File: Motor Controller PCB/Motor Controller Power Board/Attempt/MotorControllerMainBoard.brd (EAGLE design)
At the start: 70 x 100 mm, 47 parts

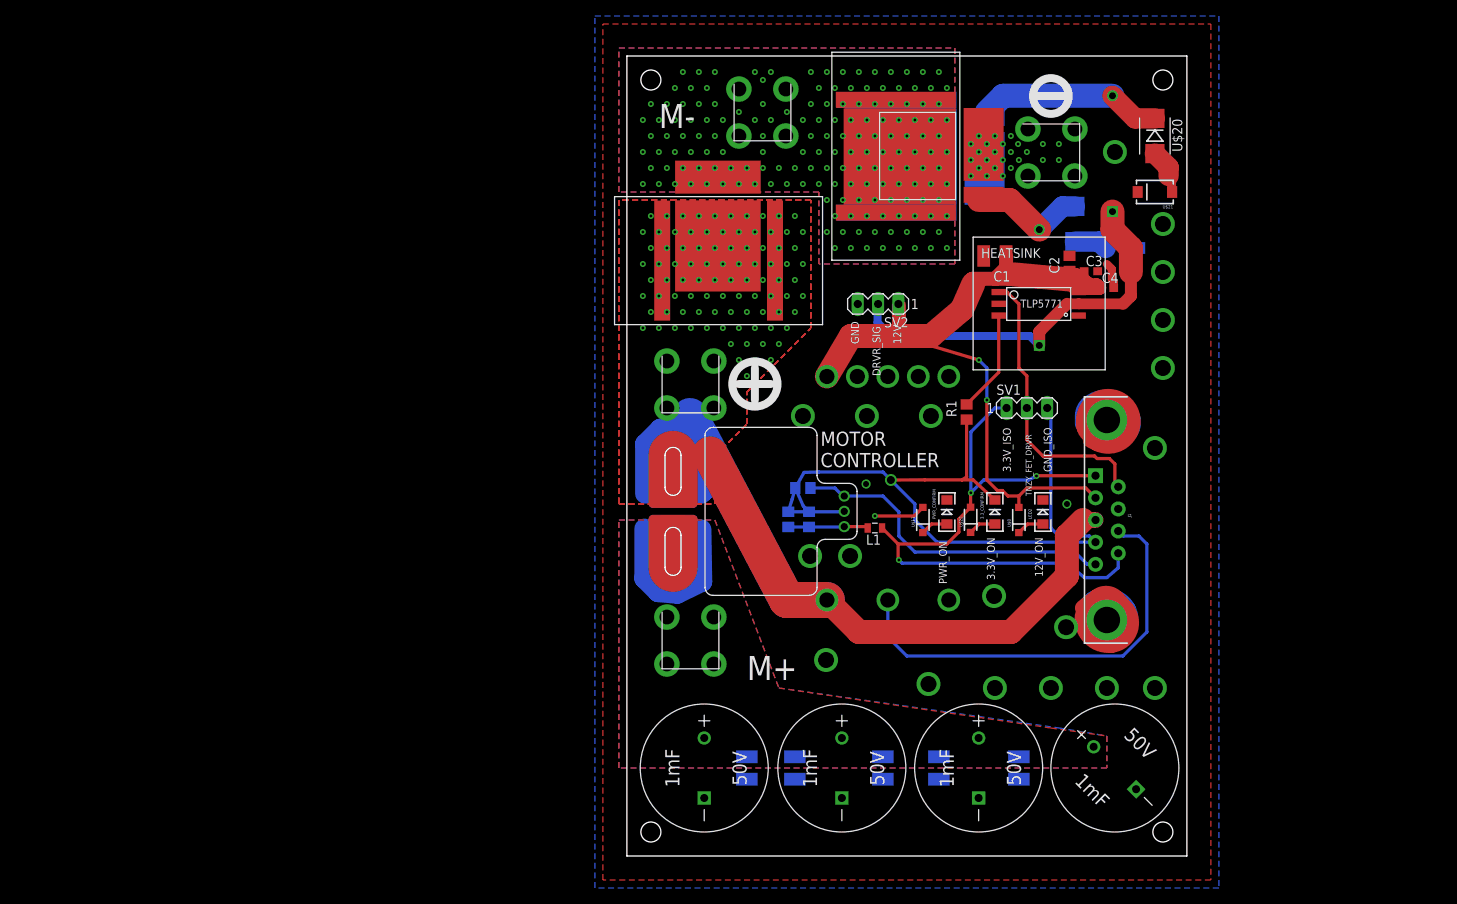
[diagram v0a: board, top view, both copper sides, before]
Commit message: Doing a new layout
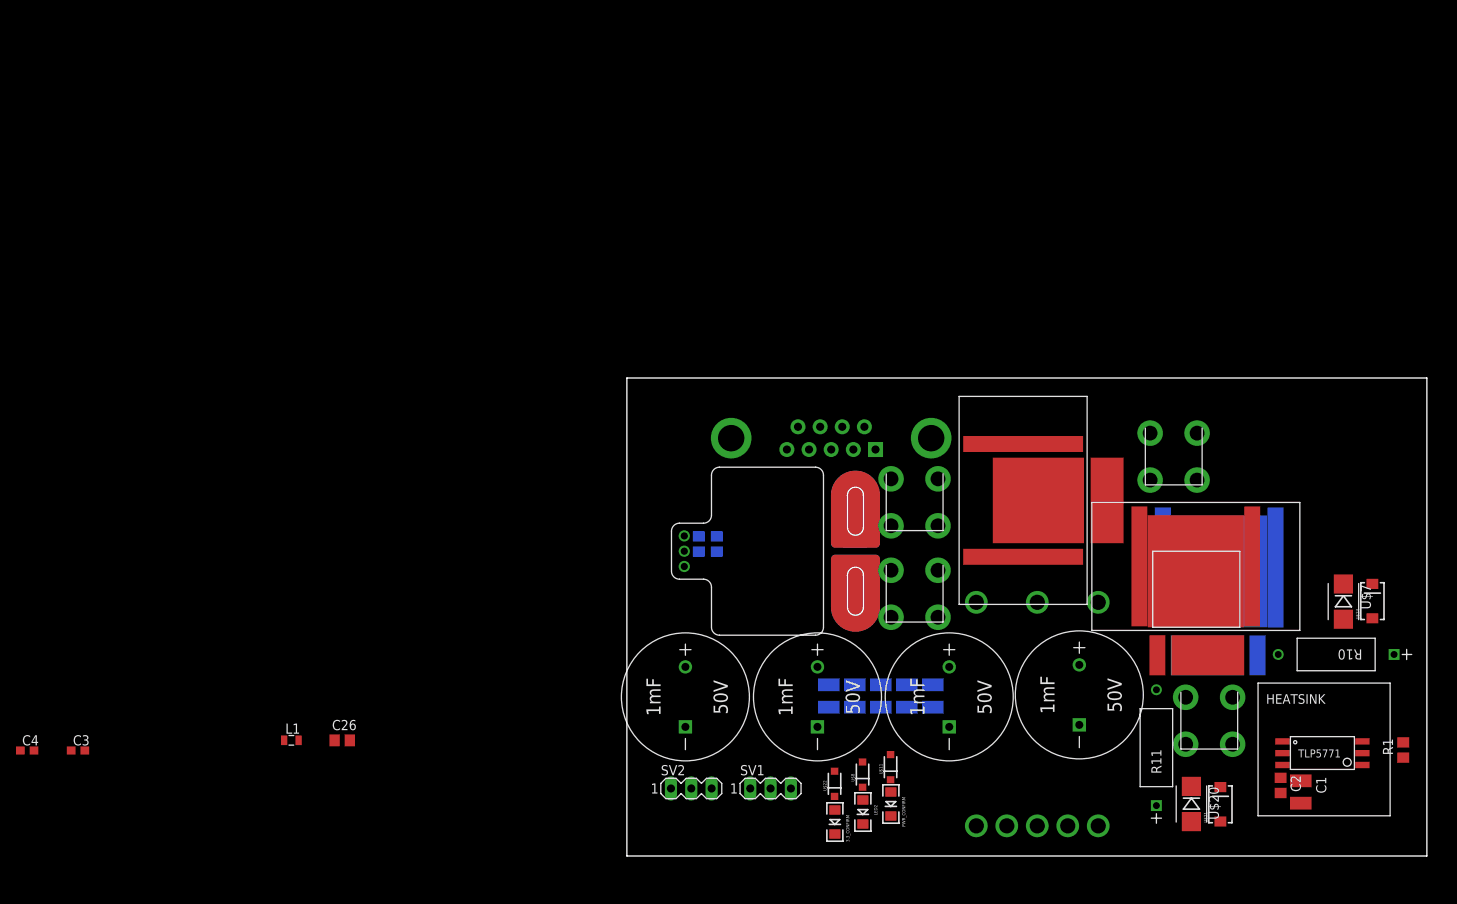
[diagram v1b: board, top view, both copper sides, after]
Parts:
- moved C4 146.8 mm to (-75.0, 13.2)
- moved C3 140.1 mm to (-68.6, 13.2)
- moved U$20 83.6 mm to (70.6, 6.50)
- moved L1 77.6 mm to (-41.9, 14.5), turned to 0 degrees
- moved C1 77.1 mm to (84.2, 8.00), turned to 270 degrees
- moved U$21 77.0 mm to (74.2, 6.46), turned to 90 degrees
- moved R11 74.5 mm to (66.2, 20.8), flipped to the top
- moved U$15 72.4 mm to (69.8, 14.0), turned to 0 degrees
- moved C2 70.4 mm to (81.7, 8.83), turned to 270 degrees
- moved R1 69.0 mm to (97.0, 13.2)
- moved U$12 67.0 mm to (65.4, 47.0)
- moved U$25 66.2 mm to (78.9, 5.03)
- moved U$2 65.7 mm to (74.0, 34.3), flipped to the bottom, turned to 0 degrees
- moved C26 65.7 mm to (-35.6, 14.5), flipped to the top
- moved U$4 65.4 mm to (74.0, 36.1), flipped to the bottom, turned to 0 degrees
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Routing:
- net INPUT_POWER(+): track 128.0 -> 0.00 mm, vias 92 -> 0
- net GND_ISOLATED: track 100.4 -> 0.00 mm, vias 1 -> 0
- net 12V_POWER_REGULATED: track 96.2 -> 0.00 mm, vias 2 -> 0
- net 3.3V_ISOLATED: track 78.8 -> 0.00 mm, vias 3 -> 0
- net GND: track 56.9 -> 0.00 mm, vias 46 -> 0
- net ENABLE_12V: track 54.5 -> 0.00 mm
- net FET_DRIVER_SIGNAL: track 50.3 -> 0.00 mm
- net CURRENT_SENSOR_OUTPUT: track 41.4 -> 0.00 mm
- net TEENSY_FET_DRIVER_SIGNAL: track 35.8 -> 0.00 mm
- net N$10: track 23.9 -> 0.00 mm
- net MOTOR_OUTPUT_(+): track 21.0 -> 0.00 mm
- net N$2: track 15.6 -> 0.00 mm
- net N$7: track 12.8 -> 0.00 mm
- net N$6: track 10.0 -> 0.00 mm
- net N$4: track 5.69 -> 0.00 mm
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- removed copper zone on layer 1, net GND
- removed copper zone on layer 16, net GND
- removed copper zone on layer 1, net INPUT_POWER(+)
- removed copper zone on layer 16, net INPUT_POWER(+)
- removed copper zone on layer 1, net MOTOR_OUTPUT_(+)
- removed copper zone on layer 16, net MOTOR_OUTPUT_(+)
- removed copper zone on layer 1, net MOTOR_OUTPUT_(--)
- removed copper zone on layer 16, net MOTOR_OUTPUT_(--)
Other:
- board size 70 x 100 mm -> 100 x 59.8 mm
- board text removed: "12V"
- board text removed: "12V_ON"
- board text removed: "2018 Koltin Kosik-Harvey"
- board text removed: "3.3V_ISO"
- board text removed: "3.3V_ON"
- board text removed: "DRVR_SIG"
- board text removed: "GND"
- board text removed: "GND_ISO"
- board text removed: "M+"
- board text removed: "M-"
- board text removed: "MOTOR CONTROLLER"
- board text removed: "PWR_ON"
- board text removed: "TNZY_FET_DRVR"

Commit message: Started routing new layout
think this is the one bois
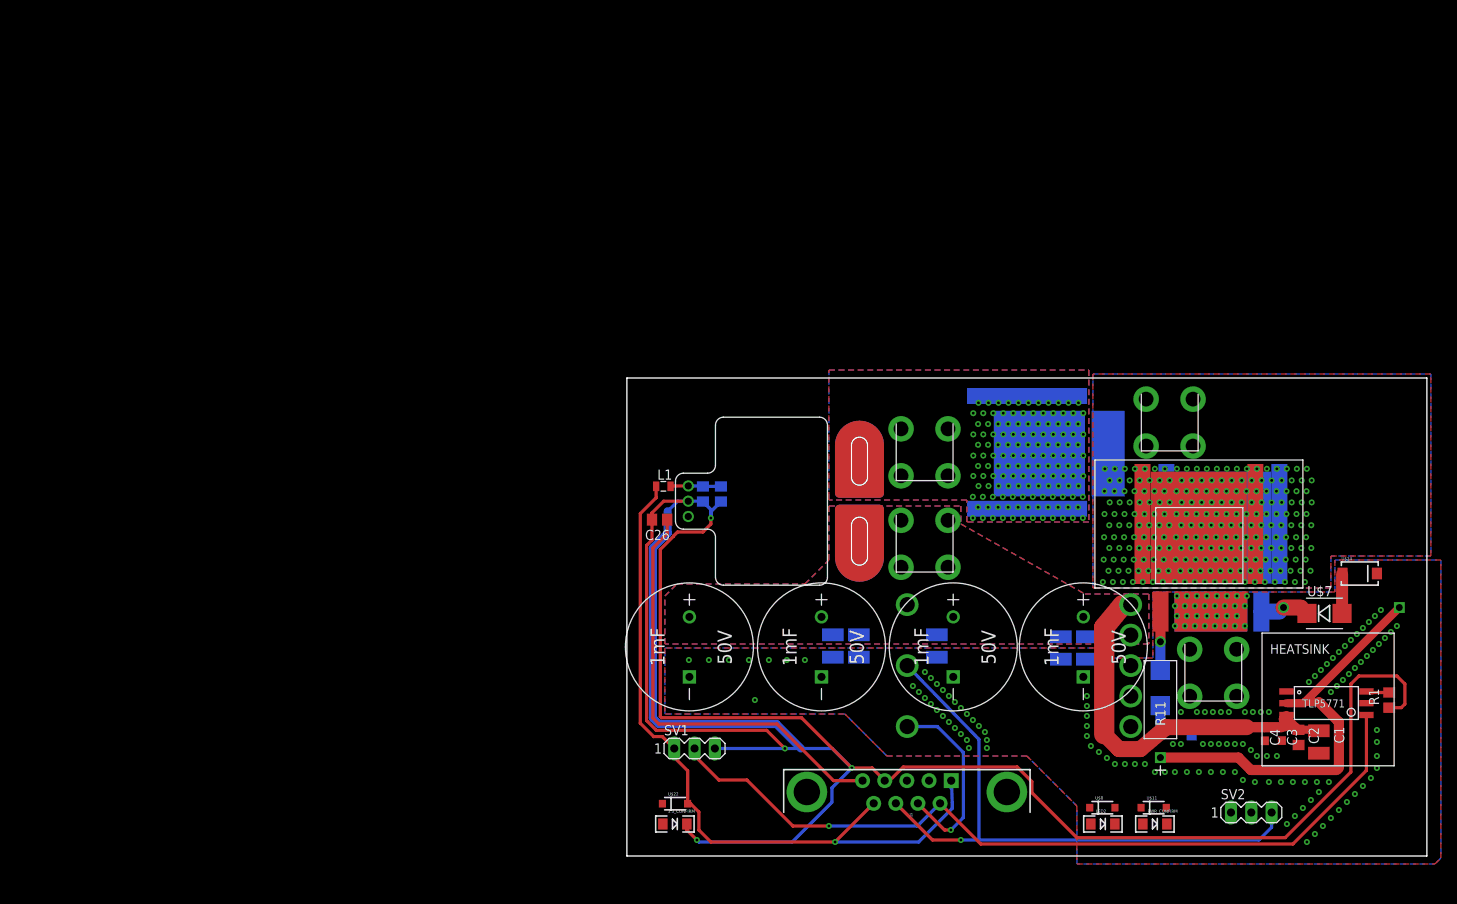
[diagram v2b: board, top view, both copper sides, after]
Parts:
- moved C4 154.7 mm to (79.8, 15.2), turned to 270 degrees
- moved C3 150.5 mm to (81.9, 15.3), turned to 270 degrees
- moved SV2 70.1 mm to (78.0, 5.44)
- moved L1 56.3 mm to (4.56, 46.2)
- moved C26 48.3 mm to (4.09, 42.0), turned to 180 degrees
- moved J1 45.2 mm to (35.0, 8.00), flipped to the top, turned to 180 degrees
- moved U$11 33.3 mm to (65.8, 6.04), turned to 0 degrees
- moved PWR_CONFIRM 33.1 mm to (66.0, 4.00), turned to 0 degrees
- moved U$8 30.3 mm to (59.4, 6.04), turned to 0 degrees
- moved LED2 30.0 mm to (59.5, 4.00), turned to 0 degrees
- moved C36 26.4 mm to (57.5, 26.0)
- moved U$6 23.9 mm to (35.0, 31.4), turned to 180 degrees
- moved C37 20.2 mm to (54.2, 26.0)
- moved U$22 20.1 mm to (6.02, 6.54), turned to 0 degrees
- moved 3.3_CONFIRM 20.0 mm to (6.00, 4.00), turned to 0 degrees
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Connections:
- net ENABLE_12V: now also SV2.3
- net GND: no longer SV2.3
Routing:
- net GND_ISOLATED: track 0.00 -> 302.5 mm, vias 0 -> 4
- net TEENSY_FET_DRIVER_SIGNAL: track 0.00 -> 102.5 mm, vias 0 -> 1
- net 3.3V_ISOLATED: track 0.00 -> 92.1 mm, vias 0 -> 1
- net ENABLE_12V: track 0.00 -> 76.8 mm, vias 0 -> 1
- net CURRENT_SENSOR_OUTPUT: track 0.00 -> 55.0 mm
- net FET_DRIVER_SIGNAL: track 0.00 -> 53.2 mm
- net 12V_POWER_REGULATED: track 0.00 -> 50.1 mm
- net GND: track 0.00 -> 24.2 mm, vias 0 -> 157
- net N$10: track 0.00 -> 7.36 mm
- net N$6: track 0.00 -> 6.34 mm
- net N$2: track 0.00 -> 6.22 mm
- net N$1: track 0.00 -> 5.01 mm
- net N$4: track 0.00 -> 3.76 mm
- net N$7: track 0.00 -> 2.90 mm
- added copper zone on layer 1, net GND
- added copper zone on layer 16, net GND
- added copper zone on layer 1, net INPUT_POWER(+)
- added copper zone on layer 16, net INPUT_POWER(+)
- added copper zone on layer 1, net MOTOR_OUTPUT_(+)
- added copper zone on layer 16, net MOTOR_OUTPUT_(+)
- added copper zone on layer 1, net MOTOR_OUTPUT_(--)
- added copper zone on layer 16, net MOTOR_OUTPUT_(--)

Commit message: More PCB Progress
I connected traces together. Hard to explain
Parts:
- moved PWR_CONFIRM 78.3 mm to (5.50, 53.8)
- moved U$11 78.3 mm to (5.35, 55.8)
- moved C36 19.3 mm to (38.2, 26.2)
- moved C38 18.0 mm to (20.8, 26.2)
- moved U$18 2.25 mm to (57.1, 23.9)
- moved U$19 2.25 mm to (40.8, 23.9)
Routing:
- net INPUT_POWER(+): track 0.00 -> 110.3 mm
- net 12V_POWER_REGULATED: track 50.1 -> 83.2 mm, vias 0 -> 1
- net N$14: track 0.00 -> 2.56 mm
- net N$9: track 0.00 -> 2.10 mm
- net GND: vias 157 -> 176
